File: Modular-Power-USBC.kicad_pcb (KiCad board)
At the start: 2 copper layers, 16 parts, among them J1 USB_C_Receptacle_PowerOnly_6P, J2 +12v Rail, J3 -12V Rail, U1 LM66100DCK

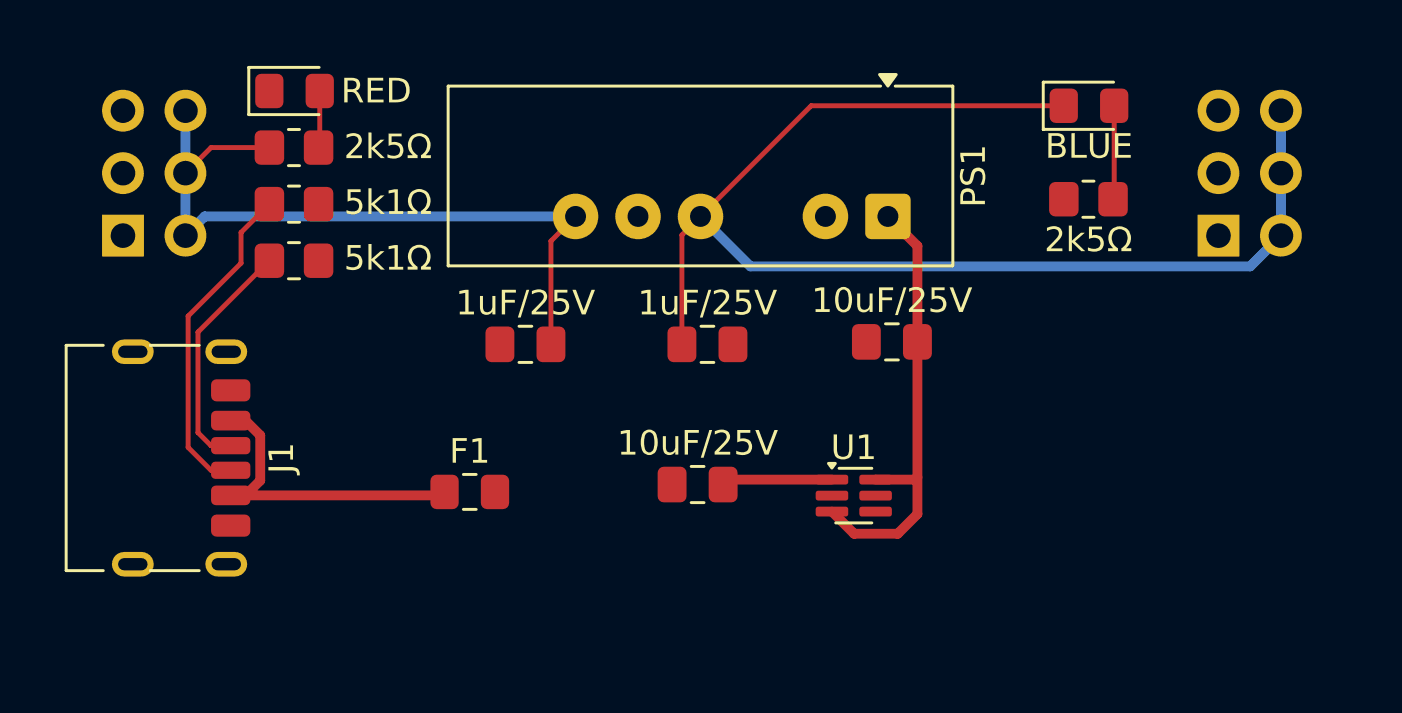
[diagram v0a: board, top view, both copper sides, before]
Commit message: Add switch
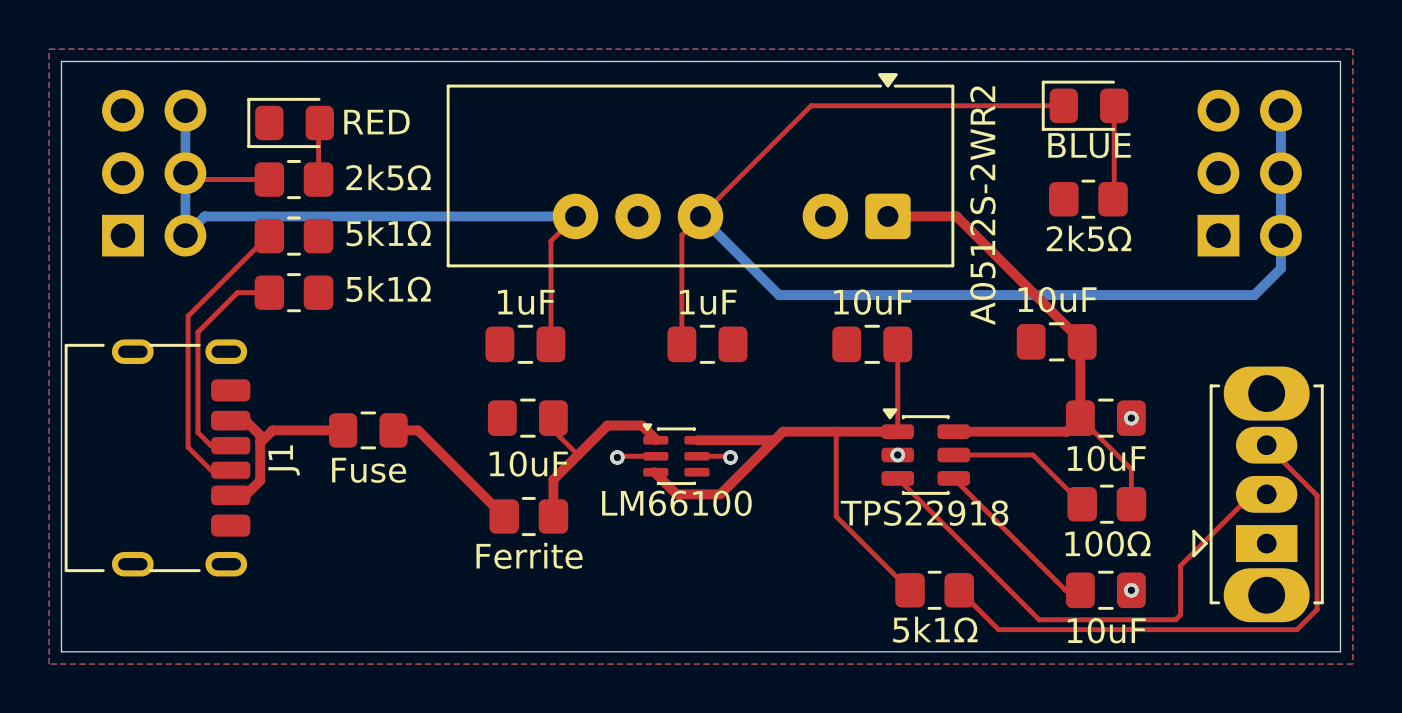
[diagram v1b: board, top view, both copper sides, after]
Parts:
- added C2: 10uF, Capacitor_SMD:C_0805_2012Metric_Pad1.18x1.45mm_HandSolder, F.Cu at (80.5, 59.5)
- added C6: 10uF, Capacitor_SMD:C_0805_2012Metric_Pad1.18x1.45mm_HandSolder, F.Cu at (90.0, 69.5)
- added C7: 10uF, Capacitor_SMD:C_0805_2012Metric_Pad1.18x1.45mm_HandSolder, F.Cu at (90.0, 62.5)
- added FB1: Ferrite, Modular-Power-USBC:FerriteBead_0805_2012Metric_Pad1.20x1.40mm_HandSolder, F.Cu at (66.5, 66.5)
- added R5: 5k1Ω, Resistor_SMD:R_0805_2012Metric_Pad1.20x1.40mm_HandSolder, F.Cu at (83.0, 69.5)
- added R6: 100Ω, Resistor_SMD:R_0805_2012Metric_Pad1.20x1.40mm_HandSolder, F.Cu at (90.0, 66.0)
- added SW1: SW_SPDT, Button_Switch_THT:SW_Slide_SPDT_Straight_CK_OS102011MS2Q, F.Cu at (96.5, 67.6)
- added U2: TPS22918, Package_TO_SOT_SMD:SOT-23-6, F.Cu at (82.6, 64.0)
- C1, C3: value 10uF/25V -> 10uF
- C4, C5: value 1uF/25V -> 1uF
- F1: value Polyfuse -> Fuse
- U1: value LM66100DCK -> LM66100
- moved C1 7.41 mm to (66.5, 62.5)
- moved U1 7.39 mm to (72.5, 64.0)
- moved C3 6.70 mm to (88.0, 59.4)
- moved F1 4.82 mm to (60.0, 63.0)
- moved R1 1.30 mm to (57.0, 55.1)
- moved D1 1.30 mm to (57.0, 50.5)
- moved R2 1.30 mm to (57.0, 57.4)
- moved R3 1.30 mm to (57.0, 52.8)
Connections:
- U1 pad 3: +5V -> /VBUS_Protected
- U1 pad 6: +5V -> /VBUS_Protected
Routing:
- net /VBUS_Protected: track 0.00 -> 25.7 mm
- net Net-(SW1-C): track 0.00 -> 23.1 mm
- net Net-(SW1-B): track 0.00 -> 20.7 mm
- net Net-(U2-CT): track 0.00 -> 7.03 mm
- net Net-(U2-QOD): track 0.00 -> 6.05 mm
- net Net-(F1-Pad2): track 0.00 -> 5.95 mm
- net /VBUS: track 13.5 -> 8.31 mm
- net +5V: track 18.6 -> 22.9 mm
- net Net-(U1-VIN): track 4.51 -> 8.76 mm
- net GND: track 0.00 -> 2.97 mm, vias 0 -> 5
- net -12V: track 52.2 -> 53.9 mm
- net /CC2: track 13.4 -> 12.1 mm
- net /CC1: track 9.74 -> 9.20 mm
- added copper zone on B.Cu, net GND
- added copper zone on F.Cu, net GND
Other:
- board outline added: 52 x 24 mm

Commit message: Generate production files
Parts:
- moved U1 1.81 mm to (74.3, 63.6)
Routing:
- net /VBUS_Protected: track 25.7 -> 23.4 mm
- net Net-(U1-VIN): track 8.76 -> 10.7 mm

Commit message: Add README and fixup traces and symbols
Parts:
- moved D2 0.70 mm to (89.3, 50.5)
- moved R4 0.70 mm to (89.3, 54.3)
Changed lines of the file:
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@@
 	(footprint "Resistor_SMD:R_0805_2012Metric_Pad1.20x1.40mm_HandSolder"
 		(layer "F.Cu")
-		(at 89.2525 53.6)
+		(at 89.2525 54.3)
 		(descr "Resistor SMD 0805 (2012 Metric), square (rectangular) end terminal, IPC-7351 nominal with elongated pad for handsoldering. (Body size source: IPC-SM-782 page 72, https://www.pcb-3d.com/wordpress/wp-content/uploads/ipc-sm-782a_amendment_1_and_2.pdf), generated with kicad-footprint-generator")
 		(tags "resistor handsolder")
@@
 	(footprint "LED_SMD:LED_0805_2012Metric_Pad1.15x1.40mm_HandSolder"
 		(layer "F.Cu")
-		(at 89.275 49.8)
+		(at 89.275 50.5)
 		(descr "LED SMD 0805 (2012 Metric), square (rectangular) end terminal, IPC-7351 nominal, (Body size source: https://docs.google.com/spreadsheets/d/1BsfQQcO9C6DZCsRaXUlFlo91Tg2WpOkGARC1WS5S8t0/edit?usp=sharing), generated with kicad-footprint-generator")
 		(tags "LED handsolder")
@@
 	)
 	(segment
-		(start 90.3 49.8)
-		(end 90.3 53.5525)
+		(start 90.2525 54.3)
+		(end 90.2525 50.5475)
 		(width 0.2)
 		(layer "F.Cu")
@@
 	)
 	(segment
-		(start 90.3 53.5525)
-		(end 90.2525 53.6)
+		(start 90.2525 50.5475)
+		(end 90.3 50.5)
 		(width 0.2)
 		(layer "F.Cu")
@@
 	)
 	(segment
-		(start 88.25 49.8)
-		(end 77.98 49.8)
+		(start 72.725 59.5)
+		(end 72.725 55.055)
 		(width 0.2)
 		(layer "F.Cu")
@@
 	)
 	(segment
-		(start 77.98 49.8)
-		(end 73.48 54.3)
+		(start 77.28 50.5)
+		(end 88.25 50.5)
 		(width 0.2)
 		(layer "F.Cu")
@@
 	)
 	(segment
-		(start 72.725 59.5)
-		(end 72.725 55.055)
+		(start 72.725 55.055)
+		(end 73.48 54.3)
 		(width 0.2)
 		(layer "F.Cu")
@@
 	)
 	(segment
-		(start 72.725 55.055)
-		(end 73.48 54.3)
+		(start 73.48 54.3)
+		(end 77.28 50.5)
 		(width 0.2)
 		(layer "F.Cu")

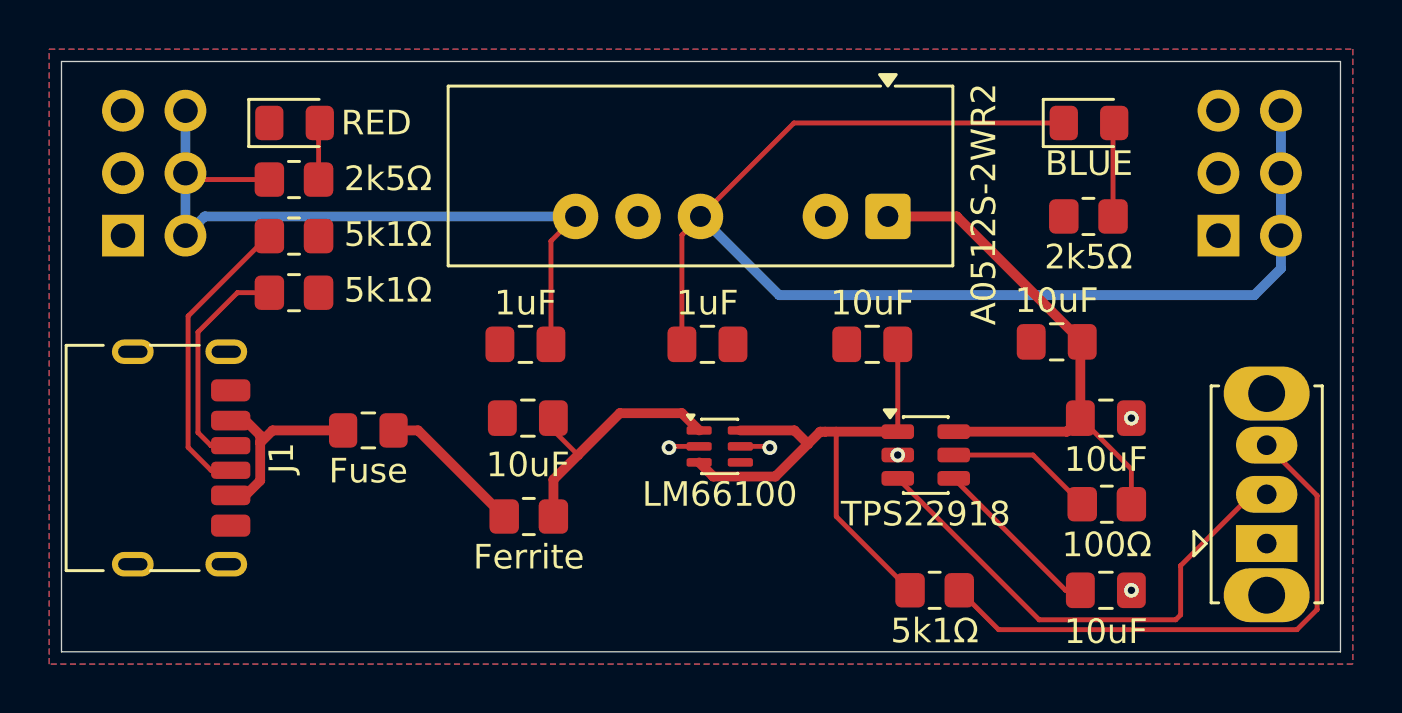
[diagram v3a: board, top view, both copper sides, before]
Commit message: Drop redundant cap
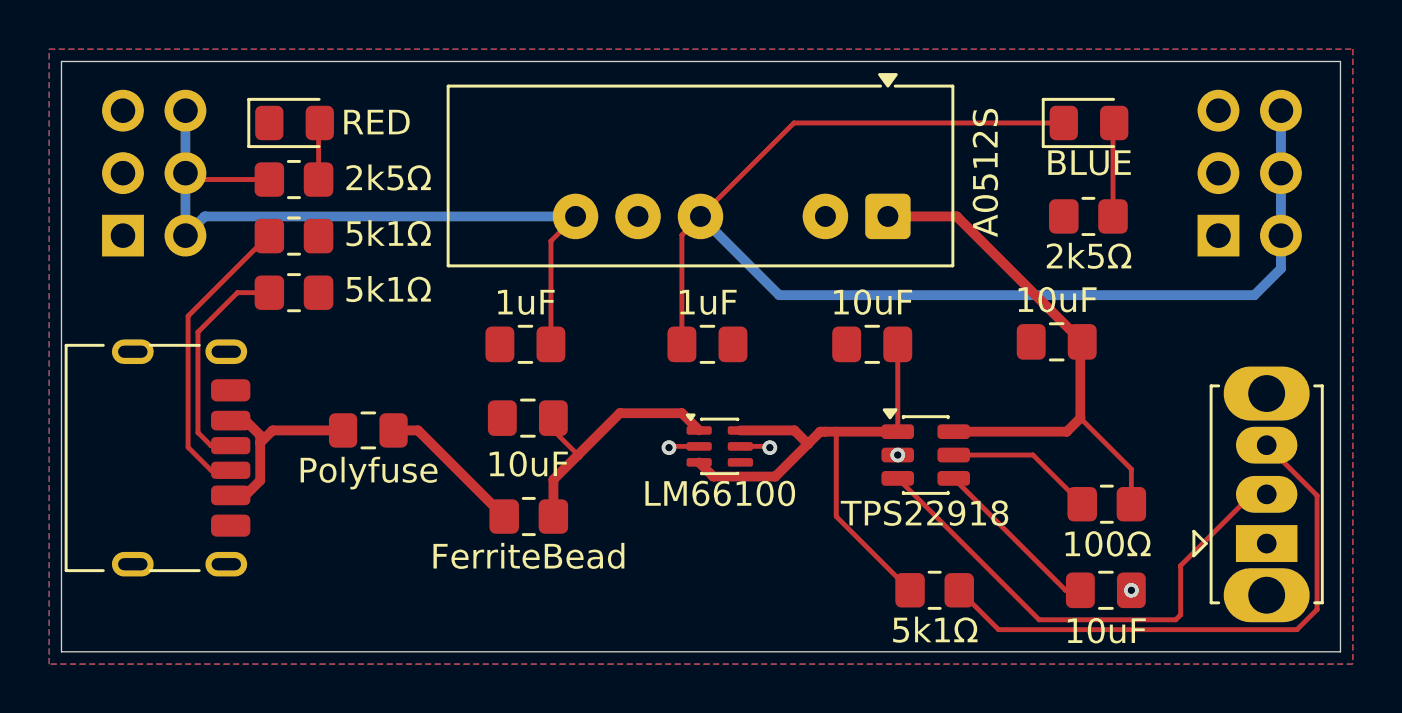
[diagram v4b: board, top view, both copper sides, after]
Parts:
- removed C7: 10uF, Capacitor_SMD:C_0805_2012Metric_Pad1.18x1.45mm_HandSolder
- F1: value Fuse -> Polyfuse
- FB1: value Ferrite -> FerriteBead
- PS1: value A0512S-2WR2 -> A0512S
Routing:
- net GND: vias 5 -> 4

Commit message: Clean up circuit with Gemini's assistance
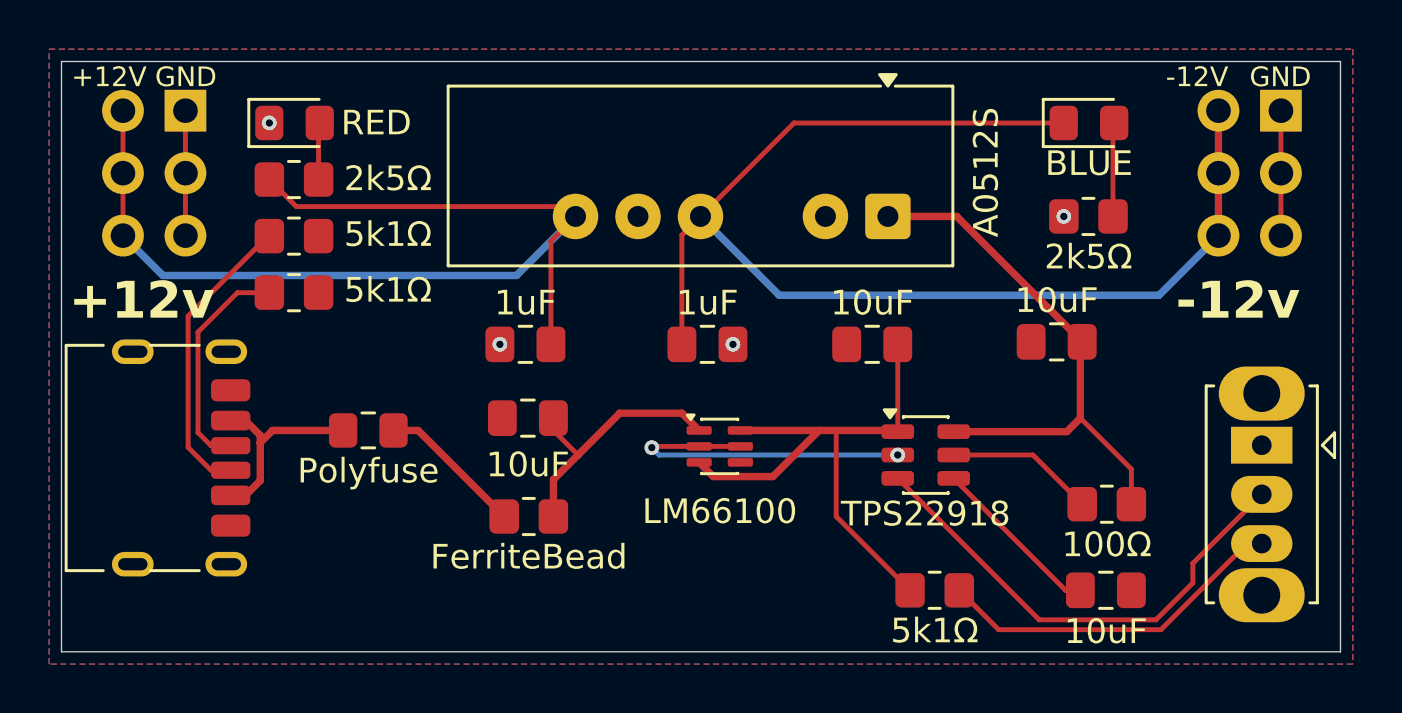
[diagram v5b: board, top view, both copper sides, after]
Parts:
- moved J2 5.68 mm to (52.5, 50.0), turned to 180 degrees
- moved J3 5.68 mm to (97.1, 50.0), turned to 180 degrees
- moved SW1 4.00 mm to (96.3, 63.6), turned to -90 degrees
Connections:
- C4 pad 2: GND -> GNDA
- C5 pad 1: GND -> GNDA
- D1 pad 1: GND -> GNDA
- J2 pad 1: GND -> GNDA
- J2 pad 3: GND -> GNDA
- J2 pad 5: GND -> GNDA
- J3 pad 1: GND -> GNDA
- J3 pad 3: GND -> GNDA
- J3 pad 5: GND -> GNDA
- PS1 pad 5: GND -> GNDA
- R4 pad 1: GND -> GNDA
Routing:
- net +12V: track 30.4 -> 43.8 mm
- net GND: track 2.47 -> 13.7 mm, vias 4 -> 2
- net GNDA: track 0.00 -> 10.5 mm, vias 0 -> 4
- net Net-(SW1-C): track 23.1 -> 14.4 mm
- net -12V: track 53.6 -> 50.3 mm
- added copper zone on B.Cu, net GNDA
- removed copper zone on B.Cu, net GND
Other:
- board text added: "+12V"
- board text added: "+12v"
- board text added: "-12V"
- board text added: "-12v"
- board text added: "GND"

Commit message: Add LCSC part numbers
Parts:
- R3, R4: value 2k5Ω -> 2k2Ω
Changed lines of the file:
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@@
 			)
 		)
-		(property "Value" "2k5Ω"
+		(property "Value" "2k2Ω"
 			(at 3.82369 -0.033333 0)
 			(layer "F.SilkS")
@@
 			)
 		)
+		(property "LCSC" "C2907303"
+			(at 0 0 0)
+			(unlocked yes)
+			(layer "F.Fab")
+			(hide yes)
+			(effects
+				(font
+					(size 1 1)
+					(thickness 0.15)
+				)
+			)
+		)
 		(property ki_fp_filters "R_*")
 		(sheetname "/")
@@
 			)
 		)
-		(property "Value" "2k5Ω"
+		(property "Value" "2k2Ω"
 			(at 0 1.65 0)
 			(layer "F.SilkS")
@@
 			)
 		)
+		(property "LCSC" "C2907303"
+			(at 0 0 0)
+			(unlocked yes)
+			(layer "F.Fab")
+			(hide yes)
+			(effects
+				(font
+					(size 1 1)
+					(thickness 0.15)
+				)
+			)
+		)
 		(property ki_fp_filters "R_*")
 		(sheetname "/")
@@
 			)
 		)
+		(property "LCSC" "C2907294"
+			(at 0 0 0)
+			(unlocked yes)
+			(layer "F.Fab")
+			(hide yes)
+			(effects
+				(font
+					(size 1 1)
+					(thickness 0.15)
+				)
+			)
+		)
 		(property ki_fp_filters "R_*")
 		(sheetname "/")
@@
 			)
 		)
+		(property "LCSC" "C84256"
+			(at 0 0 0)
+			(unlocked yes)
+			(layer "F.Fab")
+			(hide yes)
+			(effects
+				(font
+					(size 1 1)
+					(thickness 0.15)
+				)
+			)
+		)
 		(property ki_fp_filters "LED* LED_SMD:* LED_THT:*")
 		(sheetname "/")
@@
 			)
 		)
+		(property "LCSC" "C2939725"
+			(at 0 0 270)
+			(unlocked yes)
+			(layer "F.Fab")
+			(hide yes)
+			(effects
+				(font
+					(size 1 1)
+					(thickness 0.15)
+				)
+			)
+		)
 		(sheetname "/")
 		(sheetfile "Modular-Power-USBC.kicad_sch")
@@
 			)
 		)
+		(property "LCSC" "C116352"
+			(at 0 0 180)
+			(unlocked yes)
+			(layer "F.Fab")
+			(hide yes)
+			(effects
+				(font
+					(size 1 1)
+					(thickness 0.15)
+				)
+			)
+		)
 		(property ki_fp_filters "C_*")
 		(sheetname "/")
@@
 			)
 		)
+		(property "LCSC" "C84259"
+			(at 0 0 0)
+			(unlocked yes)
+			(layer "F.Fab")
+			(hide yes)
+			(effects
+				(font
+					(size 1 1)
+					(thickness 0.15)
+				)
+			)
+		)
 		(property ki_fp_filters "LED* LED_SMD:* LED_THT:*")
 		(sheetname "/")
@@
 			)
 		)
+		(property "LCSC" "C116352"
+			(at 0 0 180)
+			(unlocked yes)
+			(layer "F.Fab")
+			(hide yes)
+			(effects
+				(font
+					(size 1 1)
+					(thickness 0.15)
+				)
+			)
+		)
 		(property ki_fp_filters "C_*")
 		(sheetname "/")
@@
 			(at 1.27 2.38 0)
 			(layer "B.SilkS")
+			(hide yes)
 			(effects
 				(font
@@
 		)
 		(property "Value" "+12v Rail"
-			(at 1.27 -7.46 0)
-			(layer "B.Fab")
+			(at -2.96 -2.6 270)
+			(layer "B.SilkS")
 			(effects
 				(font
@@
 			)
 		)
+		(property "LCSC" "C7501274"
+			(at 0 0 180)
+			(unlocked yes)
+			(layer "B.Fab")
+			(hide yes)
+			(effects
+				(font
+					(size 1 1)
+					(thickness 0.15)
+				)
+				(justify mirror)
+			)
+		)
 		(property ki_fp_filters "Connector*:*_2x??_*")
 		(sheetname "/")
@@
 		(tags "Through hole pin header THT 2x03 2.54mm double row")
 		(property "Reference" "J3"
-			(at 1.27 2.38 0)
+			(at 5.48 -1.8 0)
 			(layer "B.SilkS")
+			(hide yes)
 			(effects
 				(font
@@
 		)
 		(property "Value" "-12V Rail"
-			(at 1.27 -7.46 0)
-			(layer "B.Fab")
+			(at 5.28 -2.5 270)
+			(layer "B.SilkS")
 			(effects
 				(font
@@
 					(thickness 0.15)
 				)
+				(justify mirror)
+			)
+		)
+		(property "LCSC" "C7501274"
+			(at 0 0 180)
+			(unlocked yes)
+			(layer "B.Fab")
+			(hide yes)
+			(effects
+				(font
+					(size 1 1)
+					(thickness 0.15)
+				)

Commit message: Update for production
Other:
- board text added: "https://github.com/domesticmouse/Modular-Power-USBC"
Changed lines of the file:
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@@
 			)
 		)
-		(property "LCSC" "C76818"
+		(property "LCSC" "C307778"
 			(at 0 0 0)
 			(unlocked yes)
@@
 		)
 	)
+	(gr_text "https://github.com/domesticmouse/Modular-Power-USBC"
+		(at 70.69 71.02 0)
+		(layer "B.SilkS")
+		(effects
+			(font
+				(size 1 1)
+				(thickness 0.1)
+			)
+			(justify bottom mirror)
+		)
+	)
